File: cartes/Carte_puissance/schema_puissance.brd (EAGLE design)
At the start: 73.7 x 46.6 mm, 25 parts, among them X1 MICROMATCH-8, X2 GMSTBA2

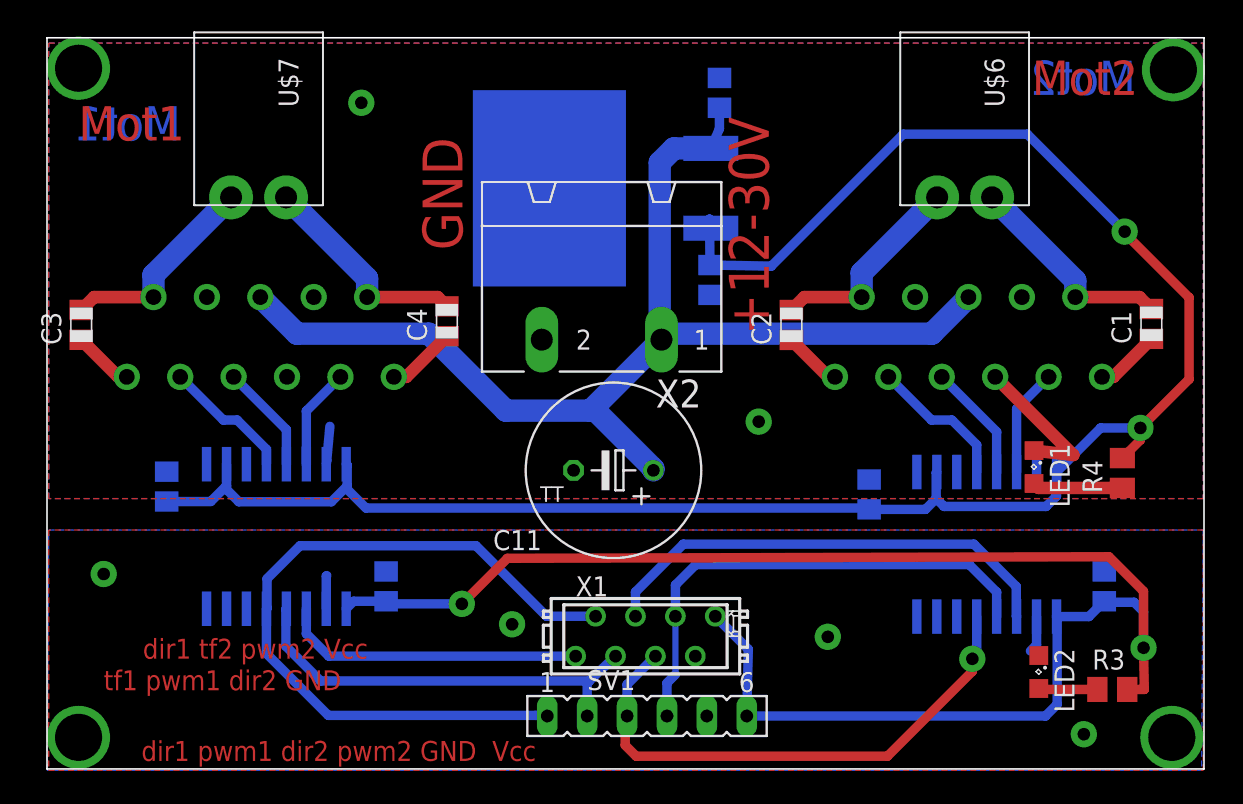
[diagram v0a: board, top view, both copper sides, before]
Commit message: Ajout carte puissance
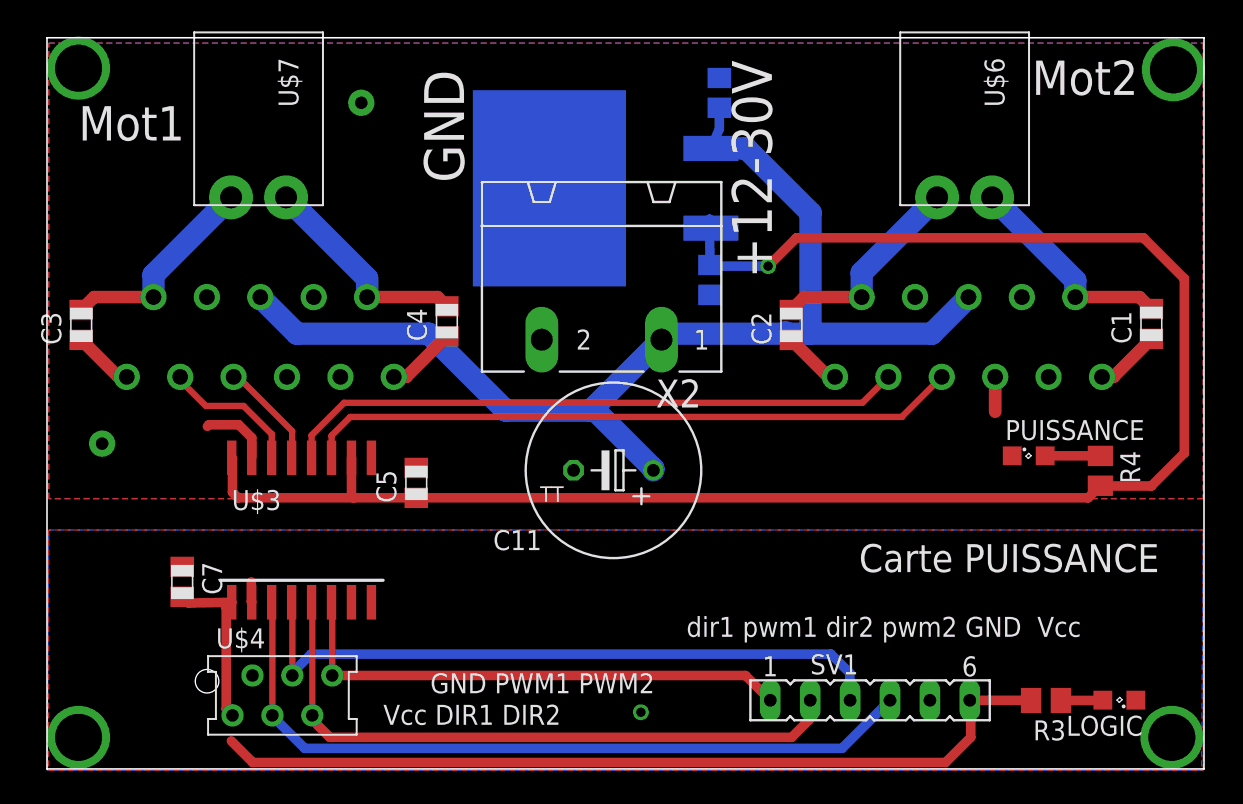
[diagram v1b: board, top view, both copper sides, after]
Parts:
- removed C6, C8: 100nF, rcl:C0805
- removed LED1, LED2: (no value), led:SML0805
- removed X1: MICROMATCH-8, con-amp-micromatch:MICROMATCH-8
- added LOGIC, PUISSANCE: (no value), led:SML0805
- U$4: value ADUM1400S -> MMATCH-6-; device analog-devices:SO-16W -> jt-con-micromatch:AMP-215079-6
- moved U$3 43.6 mm to (25.1, 22.0), flipped to the top
- moved C5 15.9 mm to (32.4, 25.0), flipped to the top
- moved SV1 14.2 mm to (61.3, 11.2)
- moved C7 13.0 mm to (17.5, 18.7), flipped to the top
- moved U$4 11.7 mm to (20.7, 10.2), flipped to the top
- moved R3 4.28 mm to (72.5, 11.2), turned to 180 degrees
- moved R4 1.41 mm to (76.0, 25.8), turned to 270 degrees
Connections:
- removed net C_TF1: U$4.3, X1.8
- removed net C_TF2: U$3.3, X1.5
- net +5V: no longer C6.1, U$4.10, U$4.16
- net C_DIR1: now also SV1.4, U$3.3, U$4.3; no longer SV1.1, U$4.5, X1.7
- net C_DIR2: now also SV1.2, U$4.5; no longer SV1.3, X1.4
- net C_PWM1: now also SV1.3, U$3.4; no longer SV1.2, X1.6
- net C_PWM2: now also SV1.1, U$3.6, U$4.6; no longer SV1.4, U$3.4, X1.3
- net DIR1: now also U$3.14; no longer U$4.12
- net GND: now also LOGIC.C; no longer C8.1, LED2.C, U$4.8, X1.2
- net GNDA: now also PUISSANCE.C; no longer C6.2, LED1.C, U$4.15, U$4.9
- net N$2: now also PUISSANCE.A; no longer LED1.A
- net N$4: now also LOGIC.A; no longer LED2.A
- net PWM1: now also U$3.13; no longer U$4.13
- net PWM2: now also U$3.11; no longer U$3.13
- net TF1: no longer U$4.14
- net TF2: no longer U$3.14
- net VCC: no longer C8.2, X1.1
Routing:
- net VCC: track 101.9 -> 65.4 mm, vias 2 -> 0
- net PWM2: track 7.51 -> 41.8 mm
- net DIR2: track 9.15 -> 39.7 mm
- net C_TF2: track 30.1 -> 0.00 mm
- net C_TF1: track 19.3 -> 0.00 mm
- net C_PWM1: track 27.2 -> 43.1 mm
- net +5V: track 125.9 -> 113.4 mm, vias 2 -> 1
- net TF2: track 6.90 -> 0.00 mm
- net C_DIR2: track 34.7 -> 41.4 mm, vias 1 -> 0
- net TF1: track 6.46 -> 0.00 mm
- net GNDA: track 12.0 -> 6.70 mm
- net GND: track 4.47 -> 1.31 mm, vias 6 -> 3
- net N$2: track 5.74 -> 3.51 mm
- net C_PWM2: track 31.8 -> 33.2 mm
- net N$4: track 3.75 -> 2.67 mm
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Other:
- board text added: "Carte PUISSANCE"
- board text added: "GND PWM1 PWM2 Vcc DIR1 DIR2"
- board text removed: "dir1 tf2 pwm2 Vcc tf1 pwm1 dir2 GND"
